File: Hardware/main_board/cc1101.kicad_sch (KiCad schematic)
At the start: 0 parts

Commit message: sch: done cc1101
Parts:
- added ANT1: Sub-1GHz Antenna A5, footprints:Antenna_2, symbol Library:Antenna
- added C40, C41: 100pF, symbol Device:C
- added C42: 0.6pF, symbol Device:C_Small
- added C43, C44: 9pF, symbol Device:C
- added C45, C46, C47, C48, C49, C50, C51: 100nF, symbol Device:C
- added C52, C56, C57, C62, C63, C64, C65: TBD, symbol Device:C
- added C53: 1.2pF, symbol Device:C
- added C54, C55: 10nF, symbol Device:C
- added C58, C59: 10pF, symbol Device:C
- added C60: 22pF, symbol Device:C
- added C61: 8.2pF, symbol Device:C
- added L10, L11, L13, L15, L17: 0, Inductor_SMD:L_0402_1005Metric, symbol Device:L
- added L12: 56nH, Inductor_SMD:L_0402_1005Metric, symbol Device:L
- added L14: 27nH, Inductor_SMD:L_0402_1005Metric, symbol Device:L
- added L16: 22nH, Inductor_SMD:L_0402_1005Metric, symbol Device:L
- added L18: 2.7nH, Inductor_SMD:L_0402_1005Metric, symbol Device:L
- added L19: 2.2nH, Inductor_SMD:L_0402_1005Metric, symbol Library:L
- added L20: TBD, nductor_SMD:L_0402_1005Metric, symbol Device:L
- added L8: 6.8nH, symbol Device:L
- added L9: 3.3nH, symbol Device:L
- added R16: 56K/0.1%, symbol Device:R_US
- added R17, R19: 0R, symbol Device:R_US
- added T1: B0310J50100AHF, symbol Library:B0310J50100AHF
- added TP32: CC1101_OUT, symbol Connector:TestPoint_2Pole
- added TP33: Balun, symbol Connector:TestPoint_2Pole
- added U10, U9: BGS13S4N9E6327XTSA1, symbol Library:BGS13S4N9E6327XTSA1
- added U8: CC1101RGP, Package_DFN_QFN:Texas_RGP0020H_VQFN-20-1EP_4x4mm_P0.5mm_EP2.4x2.4mm, symbol Library:CC1101RGP
- added Y3: 26MHz, symbol Device:Crystal_GND23_Small
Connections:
- new net: C41.1, C42.2, U8.12 (RF_P)
- new net: C41.2, T1.4 (Bal)
- new net: C44.2, U8.10 (XOSC_Q2), Y3.4
- new net: C40.1, C42.1, U8.13 (RF_N)
- new net: R16.1, U8.17 (RBIAS)
- new net: C45.1, U8.5 (DCOUPL)
- new net: C43.2, U8.8 (XOSC_Q1), Y3.1
- new net: C62.2, L18.2, U10.2 (RF3)
- new net: L16.2, U10.3 (RF1)
- new net: C63.1, L19.1, L20.2, U10.4 (RFIN)
- new net: L12.2, U10.5 (RF2)
- new net: C53.2, L8.2, R17.1
- new net: ANT1.1 (A), C64.2, R19.2, TP32.2
- new net: L10.1, U9.3 (RF1)
- new net: C56.1, L10.2, L11.1
- new net: C61.2, L17.2, L18.1
- new net: C60.2, L15.2, L16.1
- new net: L17.1, U9.2 (RF3)
- new net: C65.2, L19.2, R19.1
- new net: C57.1, L11.2, L12.1
- new net: C59.2, L14.2, L15.1
- new net: C40.2, T1.3 (Bal)
- new net: C58.2, L13.2, L14.1
- new net: L9.1, T1.1 (Unbal)
- new net: C52.2, L8.1, L9.2
- new net: T1.5 (DNC), T1.6 (NC)
- new net: L13.1, U9.5 (RF2)
- new net +3.3V: C46.2, C47.2, C48.2, C49.2, C50.2, C51.2, C54.1, C55.1, U10.7 (VDD), U8.11 (AVDD), U8.14 (AVDD), U8.15 (AVDD), U8.18 (DGUARD), U8.4 (DVDD), U8.9 (AVDD), U9.7 (VDD)
- new net CC1101_CS: U8.7 (CSN)
- new net CC1101_G0: U8.6 (GDO0)
- new net CC1101_UBAL: R17.2, TP33.2, U9.4 (RFIN)
- new net GND: C43.1, C44.1, C45.2, C46.1, C47.1, C48.1, C49.1, C50.1, C51.1, C52.1, C53.1, C54.2, C55.2, C56.2, C57.2, C58.1, C59.1, C60.1, C61.1, C62.1, C63.2, C64.1, C65.1, L20.1, R16.2, T1.2 (GND), TP32.1, TP33.1, U10.6 (DGND), U10.9 (GND), U8.16 (GND), U8.19 (GND), U8.21 (EPAD), U9.6 (DGND), U9.9 (GND), Y3.2, Y3.3
- new net RF_SW_0: U10.1 (V1), U9.8 (V2)
- new net RF_SW_1: U10.8 (V2), U8.3 (GD02), U9.1 (V1)
- new net SPI_R_MISO: U8.2 (SO)
- new net SPI_R_MOSI: U8.20 (SI)
- new net SPI_R_SCK: U8.1 (SCLK)
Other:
- note added: "AVDD"
- note added: "CC1101"
- note added: "DCOUP"
- note added: "DVDD"
- note added: "FREQUENCY SELECTION"

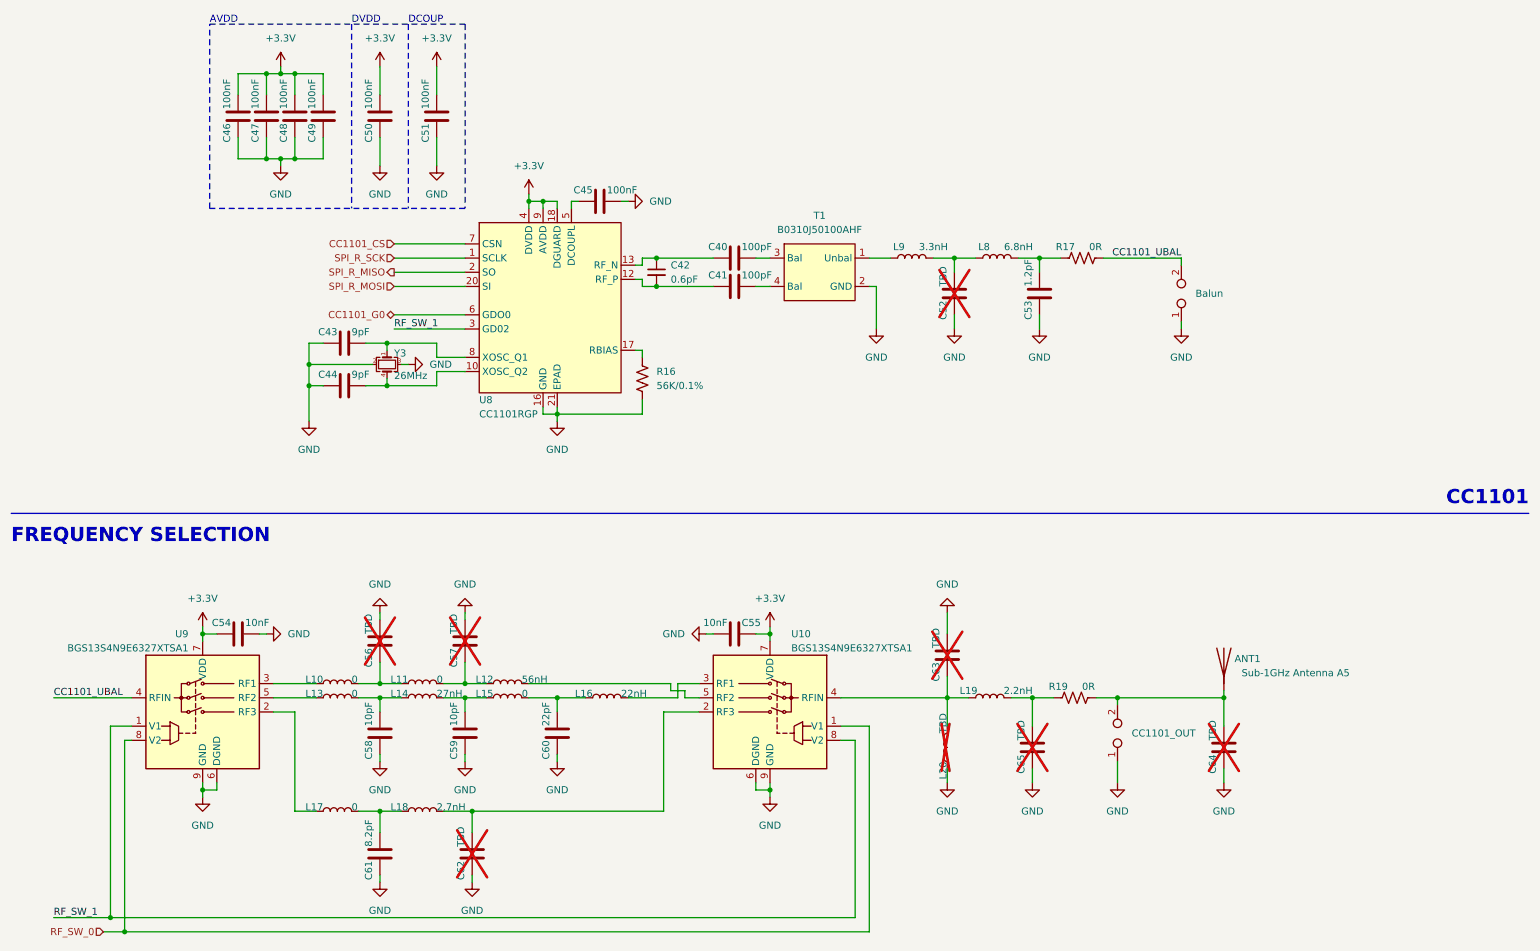
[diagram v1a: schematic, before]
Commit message: sch: add some part of footprints
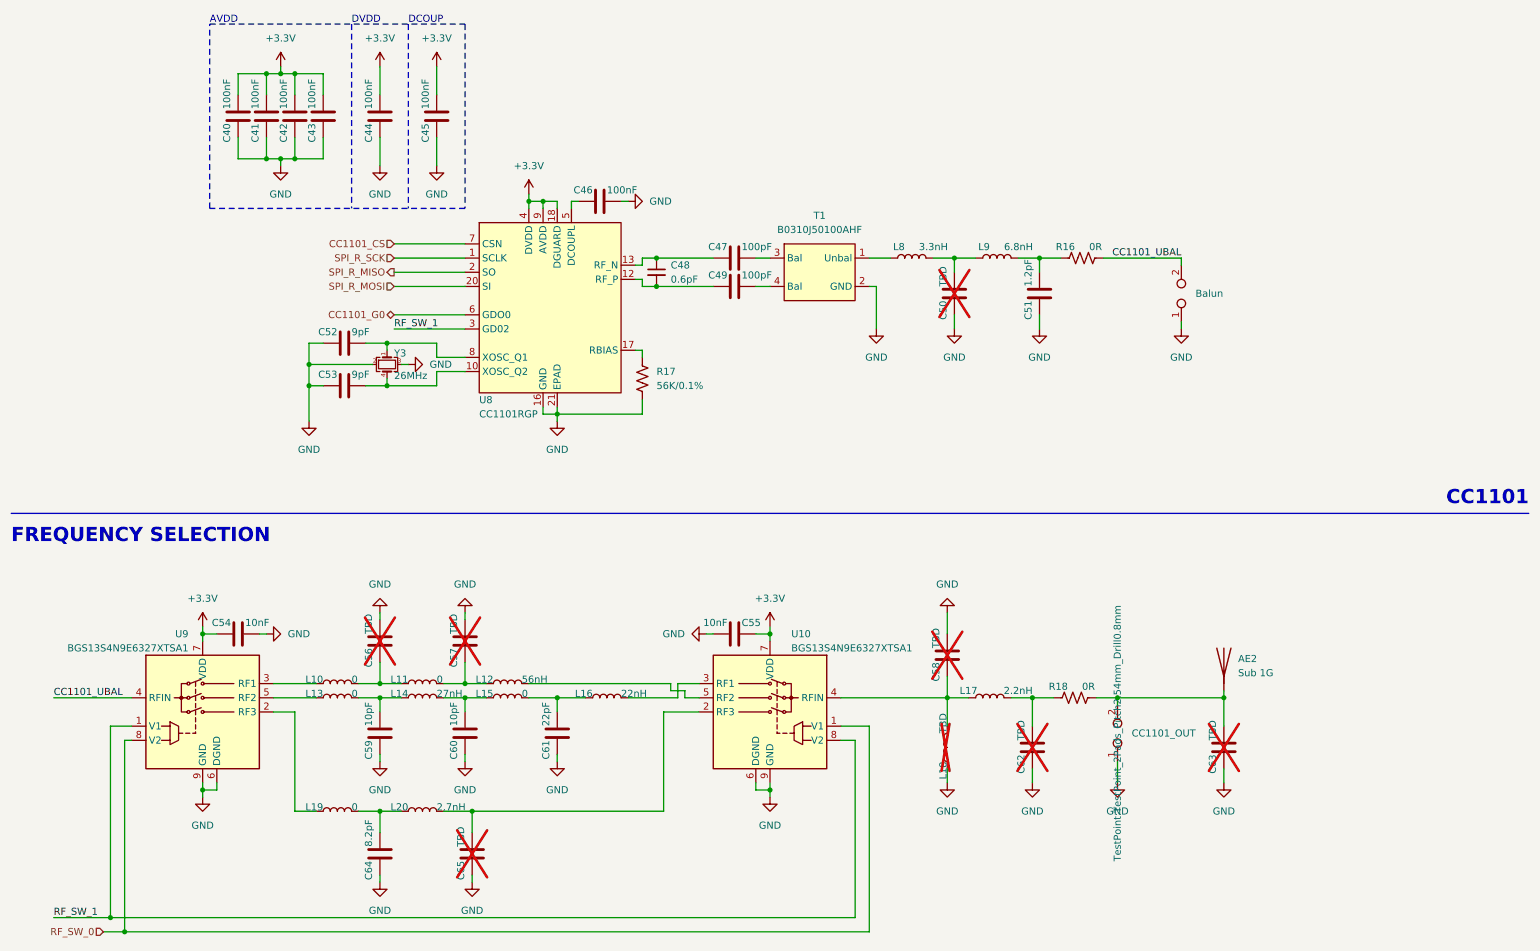
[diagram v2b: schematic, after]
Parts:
- removed ANT1: Sub-1GHz Antenna A5, footprints:Antenna_2, symbol Library:Antenna
- added AE2: Sub 1G, symbol Device:Antenna
- C40: renamed from C46; footprint (none) -> Capacitor_SMD:C_0402_1005Metric
- C41: renamed from C47; footprint (none) -> Capacitor_SMD:C_0402_1005Metric
- C42: renamed from C48; footprint (none) -> Capacitor_SMD:C_0402_1005Metric
- C43: renamed from C49; footprint (none) -> Capacitor_SMD:C_0402_1005Metric
- C44: renamed from C50; footprint (none) -> Capacitor_SMD:C_0402_1005Metric
- C45: renamed from C51; footprint (none) -> Capacitor_SMD:C_0402_1005Metric
- C46: renamed from C45; footprint (none) -> Capacitor_SMD:C_0402_1005Metric
- C47: renamed from C40; footprint (none) -> Capacitor_SMD:C_0402_1005Metric
- C48: renamed from C42; footprint (none) -> Capacitor_SMD:C_0402_1005Metric
- C49: renamed from C41; footprint (none) -> Capacitor_SMD:C_0402_1005Metric
- C50: renamed from C52; footprint (none) -> Capacitor_SMD:C_0402_1005Metric
- C51: renamed from C53; footprint (none) -> Capacitor_SMD:C_0402_1005Metric
- C52: renamed from C43; footprint (none) -> Capacitor_SMD:C_0402_1005Metric
- C53: renamed from C44; footprint (none) -> Capacitor_SMD:C_0402_1005Metric
- C54, C55, C56, C57: footprint (none) -> Capacitor_SMD:C_0402_1005Metric
- C58: renamed from C63; footprint (none) -> Capacitor_SMD:C_0402_1005Metric
- C59: renamed from C58; footprint (none) -> Capacitor_SMD:C_0402_1005Metric
- C60: renamed from C59; footprint (none) -> Capacitor_SMD:C_0402_1005Metric
- C61: renamed from C60; footprint (none) -> Capacitor_SMD:C_0402_1005Metric
- C62: renamed from C65; footprint (none) -> Capacitor_SMD:C_0402_1005Metric
- C63: renamed from C64; footprint (none) -> Capacitor_SMD:C_0402_1005Metric
- C64: renamed from C61; footprint (none) -> Capacitor_SMD:C_0402_1005Metric
- C65: renamed from C62; footprint (none) -> Capacitor_SMD:C_0402_1005Metric
- L8: renamed from L9; footprint (none) -> Inductor_SMD:L_0402_1005Metric
- L9: renamed from L8; footprint (none) -> Inductor_SMD:L_0402_1005Metric
- R16: renamed from R17; footprint (none) -> Resistor_SMD:R_0402_1005Metric
- R17: renamed from R16; footprint (none) -> Resistor_SMD:R_0402_1005Metric
- R18: renamed from R19; footprint (none) -> Resistor_SMD:R_0402_1005Metric
- TP32: renamed from TP33; footprint (none) -> TestPoint:TestPoint_2Pads_Pitch2.54mm_Drill0.8mm
- TP33: renamed from TP32; footprint (none) -> TestPoint:TestPoint_2Pads_Pitch2.54mm_Drill0.8mm
- Y3: footprint (none) -> Crystal:Crystal_SMD_2520-4Pin_2.5x2.0mm
- renumbered L19 to L17, L20 to L18, L17 to L19, L18 to L20
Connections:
- net at C63.2, R18.2, TP33.2: now also AE2.1 (A)

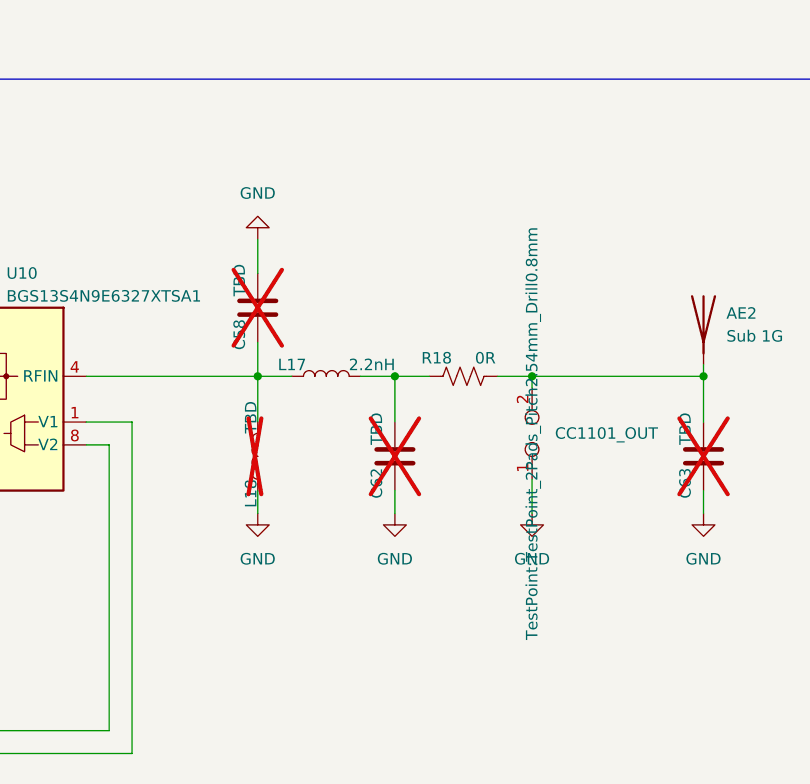
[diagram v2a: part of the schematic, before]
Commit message: sch: add more footprints
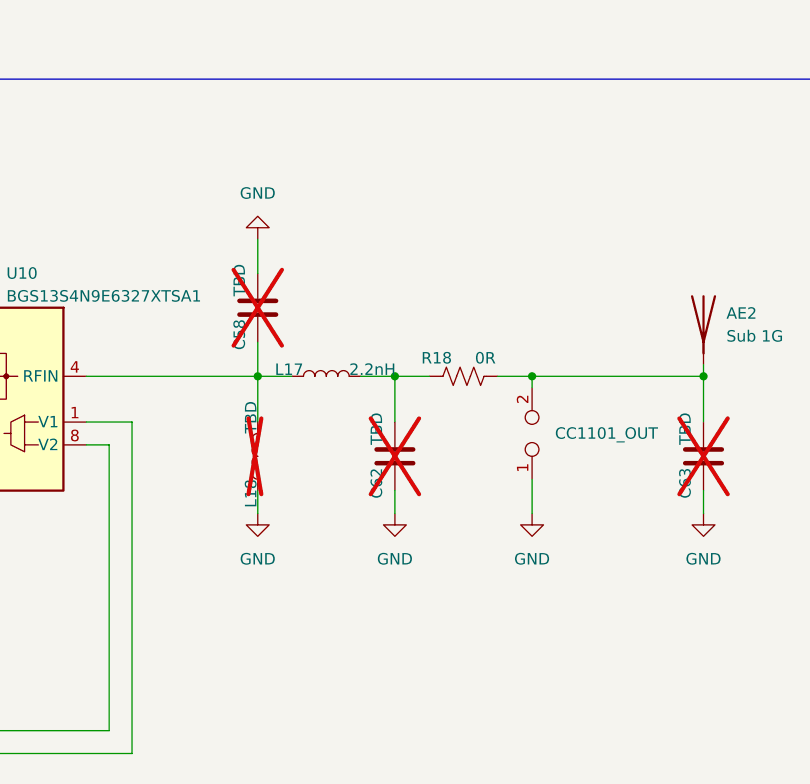
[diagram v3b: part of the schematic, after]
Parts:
- removed L17: 2.2nH, Inductor_SMD:L_0402_1005Metric, symbol Library:L
- added L17: 2.2nH, Inductor_SMD:L_0402_1005Metric, symbol Device:L
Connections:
- net at C58.1, L18.2, U10.4 (RFIN): now also L17.1
- net at C62.2, R18.1: now also L17.2
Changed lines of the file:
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@@
 			)
 		)
-		(property "Datasheet" ""
+		(property "Datasheet" "https://www.infineon.com/dgdl/Infineon-BGS13S4N9-DS-v01_00-EN.pdf"
 			(at 148.59 143.51 0)
 			(effects
@@
 					(size 1.27 1.27)
 				)
+				(hide yes)
 			)
 		)
@@
 			)
 		)
-		(property "Datasheet" ""
+		(property "Datasheet" "https://cdn.ttm.com/repository/products/wireless-xinger/balun-transformers/B0310J50100AHF/B0310J50100AHF.pdf"
 			(at 157.48 68.58 0)
 			(effects
@@
 	)
 	(symbol
+		(lib_id "Device:L")
+		(at 187.96 140.97 90)
+		(unit 1)
+		(exclude_from_sim no)
+		(in_bom yes)
+		(on_board yes)
+		(dnp no)
+		(property "Reference" "L17"
+			(at 185.42 140.97 90)
+			(effects
+				(font
+					(size 1.27 1.27)
+				)
+				(justify left top)
+			)
+		)
+		(property "Value" "2.2nH"
+			(at 190.5 140.97 90)
+			(effects
+				(font
+					(size 1.27 1.27)
+				)
+				(justify right top)
+			)
+		)
+		(property "Footprint" "Inductor_SMD:L_0402_1005Metric"
+			(at 187.96 140.97 0)
+			(effects
+				(font
+					(size 1.27 1.27)
+				)
+				(hide yes)
+			)
+		)
+		(property "Datasheet" "~"
+			(at 187.96 140.97 0)
+			(effects
+				(font
+					(size 1.27 1.27)
+				)
+				(hide yes)
+			)
+		)
+		(property "Description" "Inductor"
+			(at 187.96 140.97 0)
+			(effects
+				(font
+					(size 1.27 1.27)
+				)
+				(hide yes)
+			)
+		)
+		(pin "2"
+		)
+		(pin "1"
+		)
+		(instances
+			(project "main_board"
+				(path "/16216a68-6dea-41d7-8e15-2cc84f72f8e2/5111dc55-0d19-493a-9207-f9f348963d5b"
+					(reference "L17")
+					(unit 1)
+				)
+			)
+		)
+	)
+	(symbol
 		(lib_id "Device:C")
 		(at 78.74 147.32 180)
@@
 			)
 		)
-		(property "Datasheet" ""
+		(property "Datasheet" "https://www.infineon.com/dgdl/Infineon-BGS13S4N9-DS-v01_00-EN.pdf"
 			(at 46.99 143.51 0)
 			(effects
@@
 					(unit 1)
 				)
-			)
-		)
-	)
-	(symbol
-		(lib_id "Library:L")
-		(at 187.96 140.97 90)
-		(unit 1)
-		(exclude_from_sim no)
-		(in_bom yes)
-		(on_board yes)
-		(dnp no)
-		(property "Reference" "L17"
-			(at 184.15 139.7 90)
-			(effects
-				(font
-					(size 1.27 1.27)
-				)
-			)
-		)
-		(property "Value" "2.2nH"
-			(at 193.04 139.7 90)
-			(effects
-				(font
-					(size 1.27 1.27)
-				)
-			)
-		)
-		(property "Footprint" "Inductor_SMD:L_0402_1005Metric"
-			(at 187.96 140.97 0)
-			(effects
-				(font
-					(size 1.27 1.27)
-				)
-				(hide yes)
-			)
-		)
-		(property "Datasheet" "~"
-			(at 187.96 140.97 0)
-			(effects
-				(font
-					(size 1.27 1.27)
-				)
-				(hide yes)
-			)
-		)
-		(property "Description" ""
-			(at 187.96 140.97 0)
-			(effects
-				(font
-					(size 1.27 1.27)
-				)
-				(hide yes)
-			)
-		)
-		(pin "2"
-		)
-		(pin "1"
-		)
-		(instances
-			(project "main_board"
-				(path "/16216a68-6dea-41d7-8e15-2cc84f72f8e2/5111dc55-0d19-493a-9207-f9f348963d5b"
-					(reference "L17")
-					(unit 1)
-				)
